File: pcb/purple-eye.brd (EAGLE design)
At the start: 24.7 x 15.9 mm, 10 parts

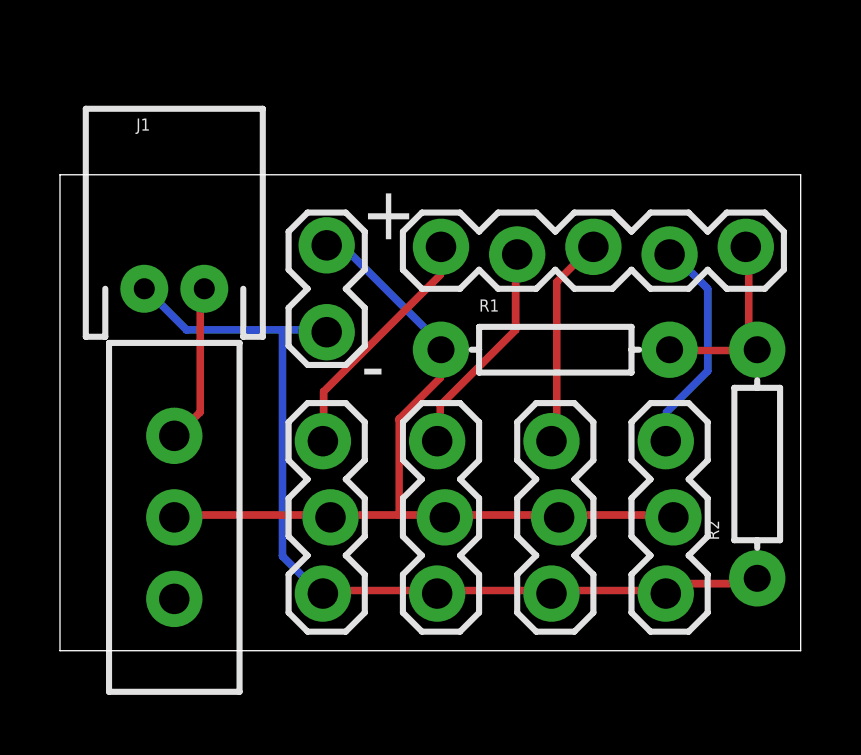
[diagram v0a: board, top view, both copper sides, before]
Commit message: feat: add charging circuit
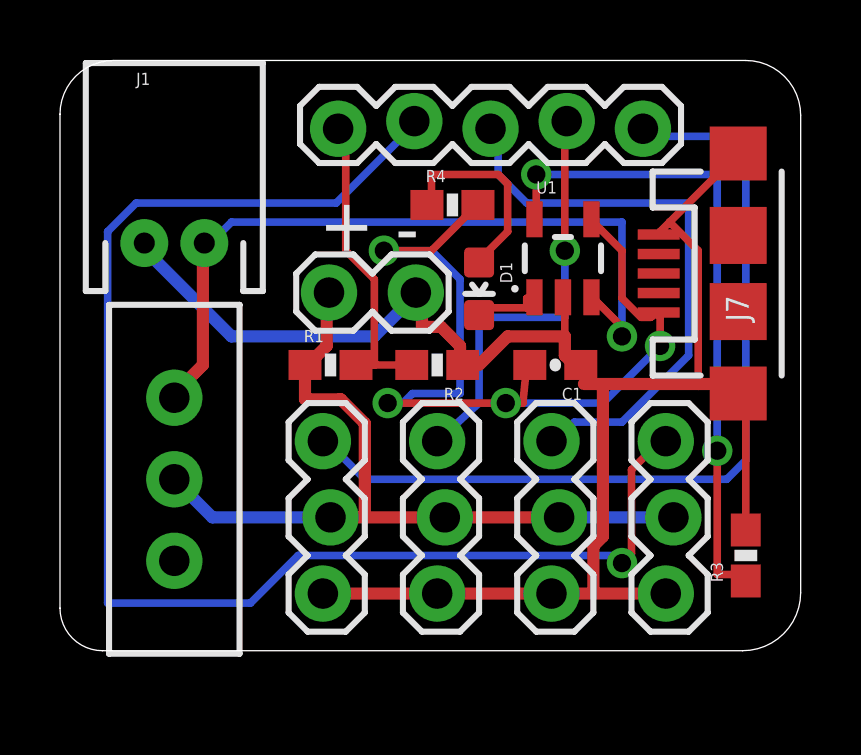
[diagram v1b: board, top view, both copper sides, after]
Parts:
- added C1: 4.7uF, SparkFun-Capacitors:0603-CAP
- added D1: RED, SparkFun-LED:LED-0603
- added J7: USB-MICROB, SparkFun-Connectors:USB-MICROB
- added R3: 2.0k, SparkFun-Resistors:0603-RES
- added R4: 4.7K, SparkFun-Resistors:0603-RES
- added U1: MCP73831, SparkFun-PowerIC:SOT23-5
- R1, R2: value 10k -> 10K; device SparkFun-Resistors:AXIAL-0.3EZ -> SparkFun-Resistors:0603-RES
- moved R2 11.2 mm to (48.1, 31.8), turned to 180 degrees
- moved J6 7.93 mm to (55.0, 39.8), turned to 180 degrees
- moved R1 7.51 mm to (44.6, 31.8)
- moved JP6 3.02 mm to (47.2, 34.2), turned to 180 degrees
- moved J1 1.52 mm to (39.4, 35.8)
- moved S1 1.27 mm to (39.4, 27.9)
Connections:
- new net N$3: D1.A, R4.1
- new net N$4: D1.C, U1.1
- new net VBAT: J1.2, S1.1, U1.3
- new net VBUS: C1.2, J7.VBUS, R4.2, U1.4
- net GND: now also C1.1, J7.GND, J7.MT1, J7.MT2, R2.1, R3.2, U1.2; no longer R2.P$1
- net N$1: now also R1.2, R2.2; no longer R1.P$2, R2.P$2
- net N$2: now also R3.1, U1.5; no longer J1.2, S1.1
- net VCC: now also R1.1; no longer R1.P$1
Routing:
- net S4: track 7.40 -> 47.0 mm, vias 0 -> 1
- net VBUS: track 0.00 -> 30.6 mm, vias 0 -> 4
- net GND: track 31.1 -> 60.1 mm
- net VBAT: track 0.00 -> 25.3 mm, vias 0 -> 1
- net S1: track 8.10 -> 29.2 mm
- net N$2: track 5.43 -> 22.0 mm, vias 0 -> 2
- net S3: track 7.14 -> 19.2 mm
- net N$3: track 0.00 -> 6.80 mm
- net S2: track 7.38 -> 14.1 mm, vias 0 -> 1
- net N$1: track 6.74 -> 10.2 mm
- net N$4: track 0.00 -> 2.41 mm
- net VCC: track 28.3 -> 26.5 mm
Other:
- board size 24.7 x 15.9 mm -> 24.7 x 19.7 mm
